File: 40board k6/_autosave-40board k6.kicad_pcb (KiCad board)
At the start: 2 copper layers, 10.1 x 6.4 mm, 111 parts, among them J1 USB_C_Receptacle_USB2.0, SW1 SW_Push, SW2 RotaryEncoder, U1 ATmega32U4-M, Y1 16MHz

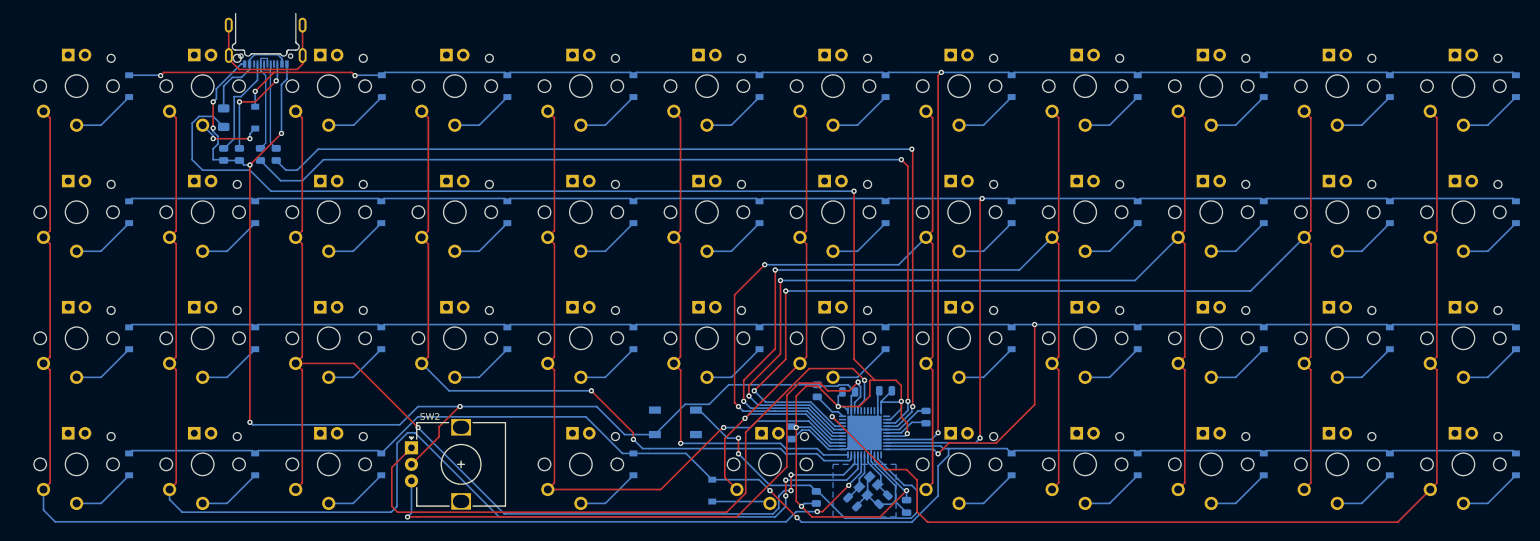
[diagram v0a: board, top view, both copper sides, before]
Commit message: Added edge cuts + ground fills
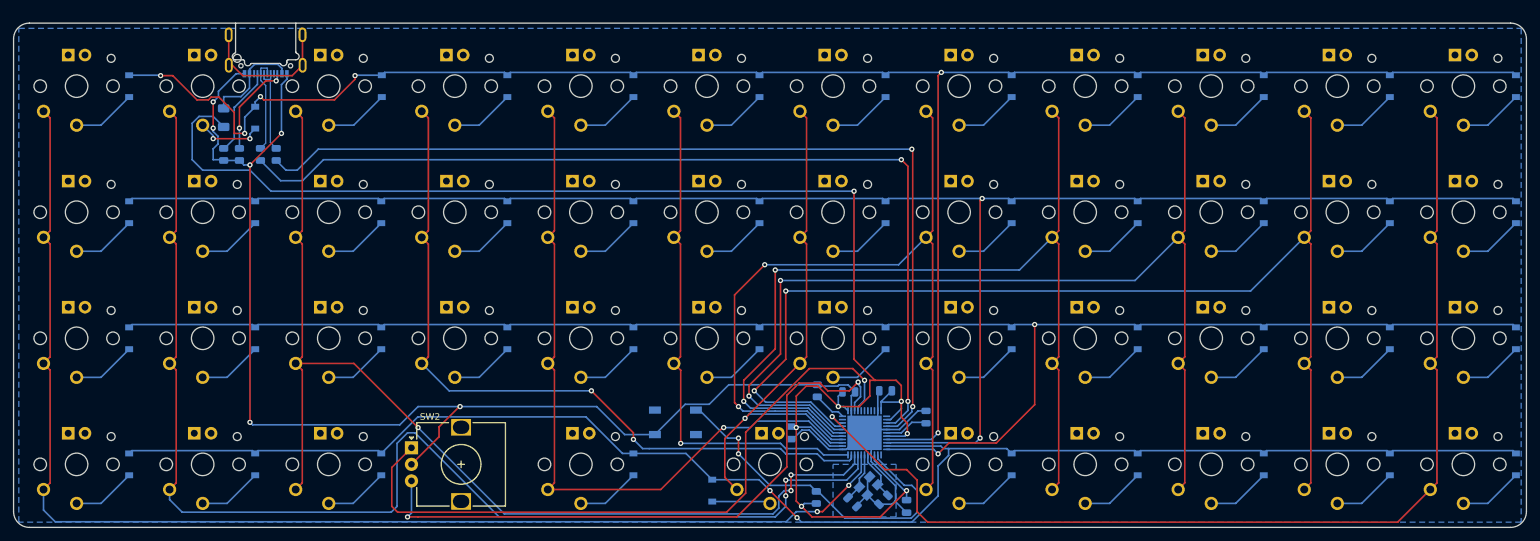
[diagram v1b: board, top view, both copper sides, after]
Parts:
- moved J1 1.47 mm to (284.2, 62.0)
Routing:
- net Row 0: track 282.4 -> 287.7 mm, vias 5 -> 6
- net GND: track 253.8 -> 251.5 mm
- net Net-(J1-PadA5): track 15.5 -> 13.5 mm
- net Net-(J1-PadB5): track 16.5 -> 14.8 mm
- net unconnected-(J1-PadS1): track 23.2 -> 21.6 mm
- net D-: track 16.0 -> 14.6 mm
- net D+: track 14.9 -> 13.4 mm
- net VCC: track 16.1 -> 15.3 mm
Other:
- board size 10.1 x 6.4 mm -> 228.6 x 76.2 mm
